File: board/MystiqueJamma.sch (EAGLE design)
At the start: 75 parts, among them IC1 7805, IC2 74LS245N, IC4 74LS245N, IC5 CY7C1049CV33, IC6 TDA1543T

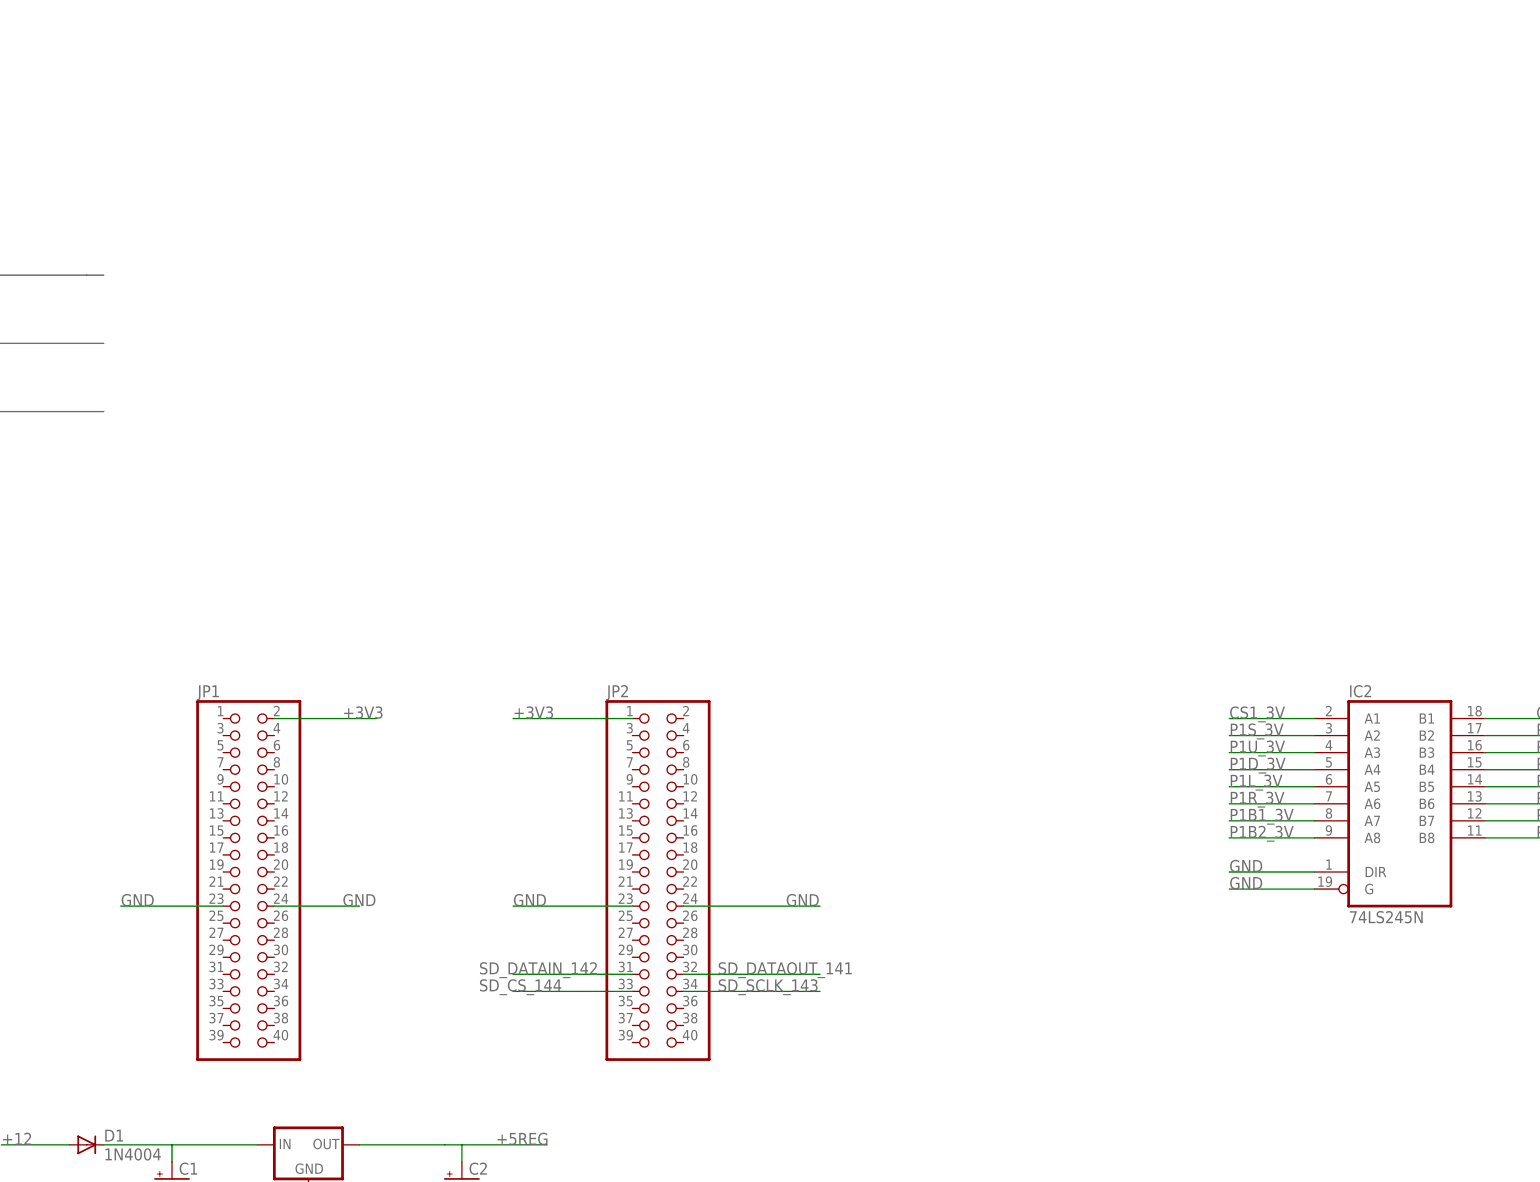
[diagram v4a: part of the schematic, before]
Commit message: included the FPGA board library
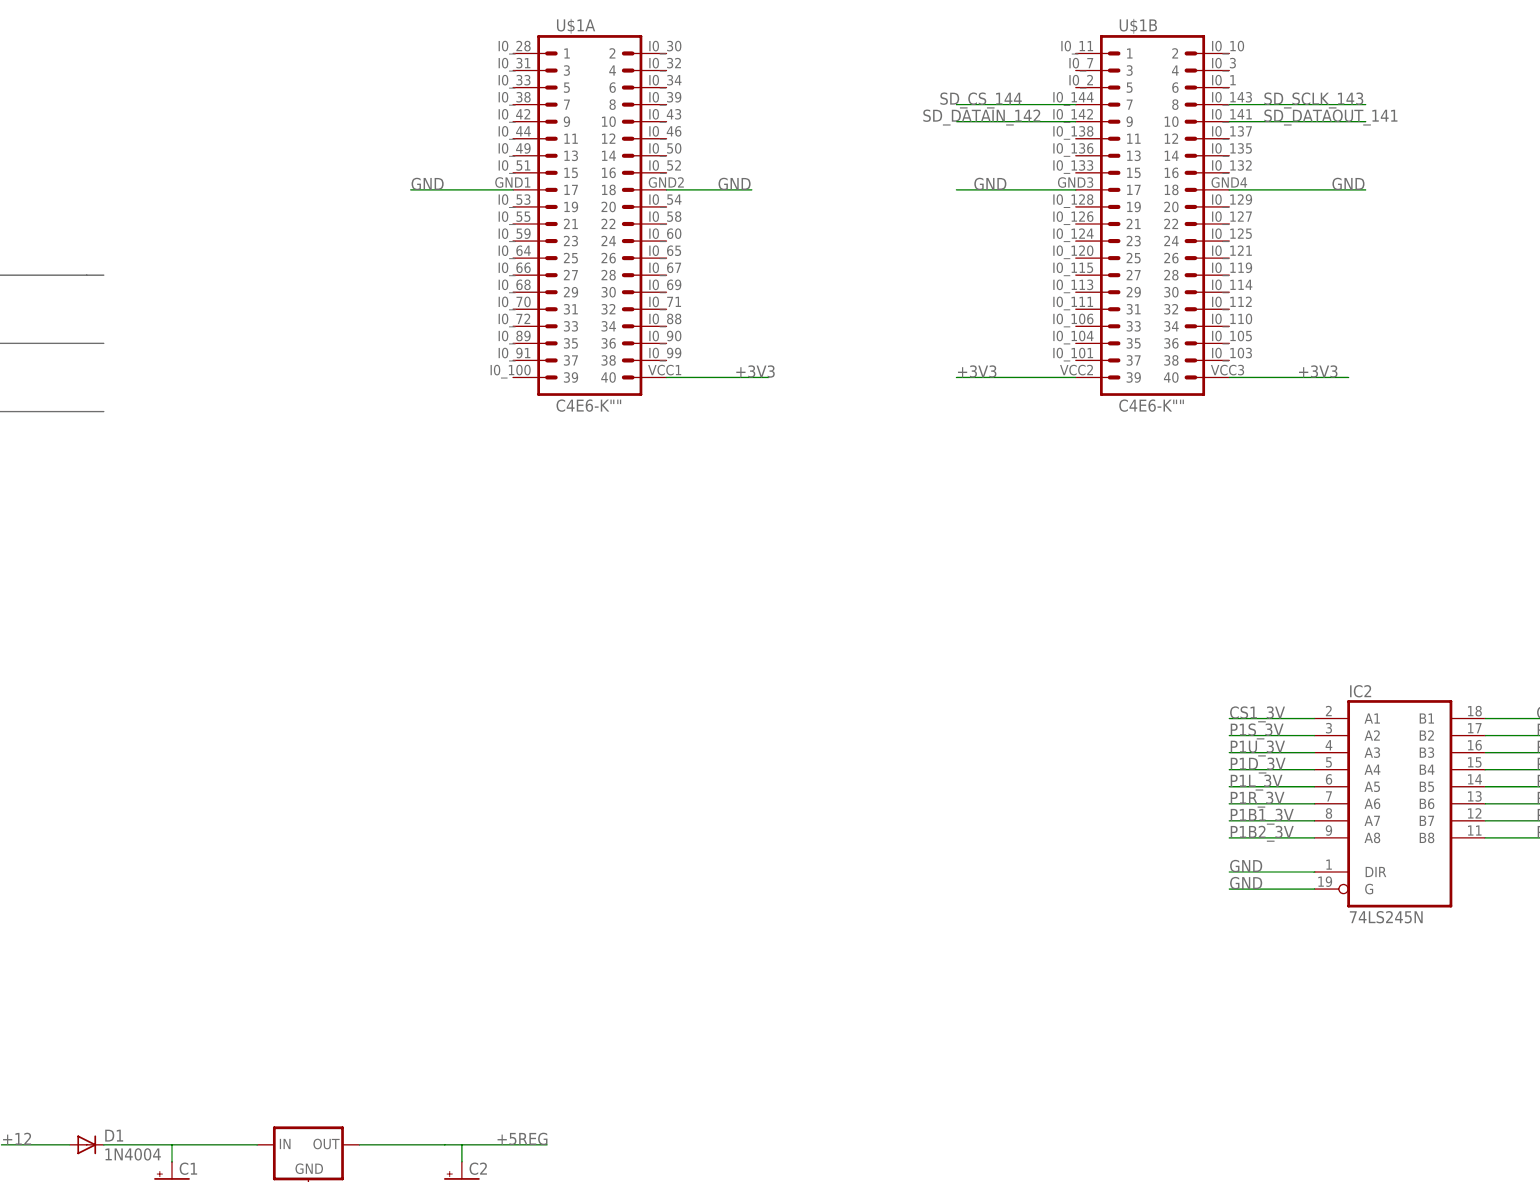
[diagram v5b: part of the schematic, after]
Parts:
- removed JP1, JP2: (no value), pinhead:PINHD-2X20
- added U$1: C4E6-K"", FPGA-BOARD:C4E6-K""
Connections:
- net +3V3: now also U$1A.40, U$1B.39; no longer JP1.2, JP2.1
- net GND: now also U$1A.17, U$1A.18, U$1B.17, U$1B.18; no longer JP1.23, JP1.24, JP2.23, JP2.24
- net SD_CS_144: now also U$1B.7; no longer JP2.33
- net SD_DATAIN_142: now also U$1B.9; no longer JP2.31
- net SD_DATAOUT_141: now also U$1B.10; no longer JP2.32
- net SD_SCLK_143: now also U$1B.8; no longer JP2.34
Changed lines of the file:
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@@
 </classes>
 <parts>
-<part name="JP1" library="pinhead" deviceset="PINHD-2X20" device=""/>
-<part name="JP2" library="pinhead" deviceset="PINHD-2X20" device=""/>
 <part name="IC1" library="SparkFun" deviceset="V_REG_78XX" device="SINK" value="7805"/>
 <part name="C1" library="rcl-2" deviceset="CPOL-US" device="E2.5-5" value="10uF"/>
@@
 <part name="R56" library="adafruit" deviceset="R-US_" device="0207/7" value="220"/>
 <part name="R57" library="adafruit" deviceset="R-US_" device="0207/7" value="220"/>
+<part name="U$1" library="FPGA-BOARD" deviceset="C4E6-K" device="&quot;&quot;"/>
 </parts>
 <sheets>
@@
 </plain>
 <instances>
-<instance part="JP1" gate="A" x="17.78" y="58.42"/>
-<instance part="JP2" gate="A" x="78.74" y="58.42"/>
 <instance part="IC1" gate="G$1" x="27.94" y="17.78"/>
 <instance part="C1" gate="G$1" x="7.62" y="12.7"/>
@@
 <instance part="R56" gate="G$1" x="-231.14" y="43.18"/>
 <instance part="R57" gate="G$1" x="-144.78" y="43.18"/>
+<instance part="U$1" gate="A" x="68.58" y="157.48"/>
+<instance part="U$1" gate="B" x="152.4" y="157.48"/>
 </instances>
 <busses>
@@
 <net name="GND" class="0">
 <segment>
-<pinref part="JP1" gate="A" pin="23"/>
-<wire x1="15.24" y1="53.34" x2="0" y2="53.34" width="0.1524" layer="91"/>
-<label x="0" y="53.34" size="1.778" layer="95"/>
-</segment>
-<segment>
-<pinref part="JP1" gate="A" pin="24"/>
-<wire x1="22.86" y1="53.34" x2="35.56" y2="53.34" width="0.1524" layer="91"/>
-<label x="33.02" y="53.34" size="1.778" layer="95"/>
-</segment>
-<segment>
-<pinref part="JP2" gate="A" pin="23"/>
-<wire x1="76.2" y1="53.34" x2="58.42" y2="53.34" width="0.1524" layer="91"/>
-<label x="58.42" y="53.34" size="1.778" layer="95"/>
-</segment>
-<segment>
-<pinref part="JP2" gate="A" pin="24"/>
-<wire x1="83.82" y1="53.34" x2="104.14" y2="53.34" width="0.1524" layer="91"/>
-<label x="99.06" y="53.34" size="1.778" layer="95"/>
+<wire x1="58.42" y1="160.02" x2="43.18" y2="160.02" width="0.1524" layer="91"/>
+<label x="43.18" y="160.02" size="1.778" layer="95"/>
+<pinref part="U$1" gate="A" pin="17"/>
+</segment>
+<segment>
+<wire x1="81.28" y1="160.02" x2="93.98" y2="160.02" width="0.1524" layer="91"/>
+<label x="88.9" y="160.02" size="1.778" layer="95"/>
+<pinref part="U$1" gate="A" pin="18"/>
+</segment>
+<segment>
+<wire x1="142.24" y1="160.02" x2="124.46" y2="160.02" width="0.1524" layer="91"/>
+<label x="127" y="160.02" size="1.778" layer="95"/>
+<pinref part="U$1" gate="B" pin="17"/>
+</segment>
+<segment>
+<wire x1="165.1" y1="160.02" x2="185.42" y2="160.02" width="0.1524" layer="91"/>
+<label x="180.34" y="160.02" size="1.778" layer="95"/>
+<pinref part="U$1" gate="B" pin="18"/>
 </segment>
 <segment>
@@
 </segment>
 <segment>
-<pinref part="JP1" gate="A" pin="2"/>
-<wire x1="22.86" y1="81.28" x2="38.1" y2="81.28" width="0.1524" layer="91"/>
-<label x="33.02" y="81.28" size="1.778" layer="95"/>
-</segment>
-<segment>
-<pinref part="JP2" gate="A" pin="1"/>
-<wire x1="76.2" y1="81.28" x2="58.42" y2="81.28" width="0.1524" layer="91"/>
-<label x="58.42" y="81.28" size="1.778" layer="95"/>
+<wire x1="81.28" y1="132.08" x2="96.52" y2="132.08" width="0.1524" layer="91"/>
+<label x="91.44" y="132.08" size="1.778" layer="95"/>
+<pinref part="U$1" gate="A" pin="40"/>
+</segment>
+<segment>
+<wire x1="142.24" y1="132.08" x2="124.46" y2="132.08" width="0.1524" layer="91"/>
+<label x="124.46" y="132.08" size="1.778" layer="95"/>
+<pinref part="U$1" gate="B" pin="39"/>
 </segment>
 <segment>
@@
 <wire x1="226.06" y1="-7.62" x2="226.06" y2="-2.54" width="0.1524" layer="91"/>
 <label x="223.52" y="-2.54" size="1.778" layer="95"/>
+</segment>
+<segment>
+<wire x1="182.88" y1="132.08" x2="165.1" y2="132.08" width="0.1524" layer="91"/>
+<label x="175.26" y="132.08" size="1.778" layer="95"/>
 </segment>
 </net>
@@
 </segment>
 <segment>
-<pinref part="JP2" gate="A" pin="33"/>
-<wire x1="76.2" y1="40.64" x2="58.42" y2="40.64" width="0.1524" layer="91"/>
-<label x="53.34" y="40.64" size="1.778" layer="95"/>
+<wire x1="142.24" y1="172.72" x2="124.46" y2="172.72" width="0.1524" layer="91"/>
+<label x="121.92" y="172.72" size="1.778" layer="95"/>
+<pinref part="U$1" gate="B" pin="7"/>
 </segment>
 </net>
@@
 </segment>
 <segment>
-<pinref part="JP2" gate="A" pin="34"/>
-<wire x1="83.82" y1="40.64" x2="104.14" y2="40.64" width="0.1524" layer="91"/>
-<label x="88.9" y="40.64" size="1.778" layer="95"/>
+<wire x1="165.1" y1="172.72" x2="185.42" y2="172.72" width="0.1524" layer="91"/>
+<label x="170.18" y="172.72" size="1.778" layer="95"/>
+<pinref part="U$1" gate="B" pin="8"/>
 </segment>
 </net>
@@
 </segment>
 <segment>
-<pinref part="JP2" gate="A" pin="31"/>
-<wire x1="76.2" y1="43.18" x2="58.42" y2="43.18" width="0.1524" layer="91"/>
-<label x="53.34" y="43.18" size="1.778" layer="95"/>
+<wire x1="142.24" y1="170.18" x2="124.46" y2="170.18" width="0.1524" layer="91"/>
+<label x="119.38" y="170.18" size="1.778" layer="95"/>
+<pinref part="U$1" gate="B" pin="9"/>
 </segment>
 </net>
@@
 </segment>
 <segment>
-<pinref part="JP2" gate="A" pin="32"/>
-<wire x1="83.82" y1="43.18" x2="104.14" y2="43.18" width="0.1524" layer="91"/>
-<label x="88.9" y="43.18" size="1.778" layer="95"/>
+<wire x1="165.1" y1="170.18" x2="185.42" y2="170.18" width="0.1524" layer="91"/>
+<label x="170.18" y="170.18" size="1.778" layer="95"/>
+<pinref part="U$1" gate="B" pin="10"/>
 </segment>
 </net>
@@
 <pinref part="R37" gate="G$1" pin="2"/>
 <junction x="-149.86" y="88.9"/>
-<pinref part="R37" gate="G$1" pin="2"/>
 <wire x1="-149.86" y1="88.9" x2="-149.86" y2="91.44" width="0.1524" layer="91"/>
 <junction x="-149.86" y="91.44"/>
@@
 <pinref part="R38" gate="G$1" pin="2"/>
 <junction x="-149.86" y="73.66"/>
-<pinref part="R38" gate="G$1" pin="2"/>
 <wire x1="-149.86" y1="73.66" x2="-149.86" y2="76.2" width="0.1524" layer="91"/>
 <junction x="-149.86" y="76.2"/>

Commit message: docs
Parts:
- B1: value C4E6-K"" -> (none)
- renumbered U$1 to B1
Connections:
- net +3V3: now also B1B.40
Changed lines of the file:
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@@
 <part name="R56" library="adafruit" deviceset="R-US_" device="0207/7" value="220"/>
 <part name="R57" library="adafruit" deviceset="R-US_" device="0207/7" value="220"/>
-<part name="U$1" library="FPGA-BOARD" deviceset="C4E6-K" device="&quot;&quot;"/>
+<part name="B1" library="FPGA-BOARD" deviceset="C4E6-K" device="&quot;&quot;"/>
 </parts>
 <sheets>
@@
 <instance part="R56" gate="G$1" x="-231.14" y="43.18"/>
 <instance part="R57" gate="G$1" x="-144.78" y="43.18"/>
-<instance part="U$1" gate="A" x="68.58" y="157.48"/>
-<instance part="U$1" gate="B" x="152.4" y="157.48"/>
+<instance part="B1" gate="A" x="68.58" y="157.48"/>
+<instance part="B1" gate="B" x="152.4" y="157.48"/>
 </instances>
 <busses>
@@
 <wire x1="58.42" y1="160.02" x2="43.18" y2="160.02" width="0.1524" layer="91"/>
 <label x="43.18" y="160.02" size="1.778" layer="95"/>
-<pinref part="U$1" gate="A" pin="17"/>
+<pinref part="B1" gate="A" pin="17"/>
 </segment>
 <segment>
 <wire x1="81.28" y1="160.02" x2="93.98" y2="160.02" width="0.1524" layer="91"/>
 <label x="88.9" y="160.02" size="1.778" layer="95"/>
-<pinref part="U$1" gate="A" pin="18"/>
+<pinref part="B1" gate="A" pin="18"/>
 </segment>
 <segment>
 <wire x1="142.24" y1="160.02" x2="124.46" y2="160.02" width="0.1524" layer="91"/>
 <label x="127" y="160.02" size="1.778" layer="95"/>
-<pinref part="U$1" gate="B" pin="17"/>
+<pinref part="B1" gate="B" pin="17"/>
 </segment>
 <segment>
 <wire x1="165.1" y1="160.02" x2="185.42" y2="160.02" width="0.1524" layer="91"/>
 <label x="180.34" y="160.02" size="1.778" layer="95"/>
-<pinref part="U$1" gate="B" pin="18"/>
+<pinref part="B1" gate="B" pin="18"/>
 </segment>
 <segment>
@@
 <wire x1="81.28" y1="132.08" x2="96.52" y2="132.08" width="0.1524" layer="91"/>
 <label x="91.44" y="132.08" size="1.778" layer="95"/>
-<pinref part="U$1" gate="A" pin="40"/>
+<pinref part="B1" gate="A" pin="40"/>
 </segment>
 <segment>
 <wire x1="142.24" y1="132.08" x2="124.46" y2="132.08" width="0.1524" layer="91"/>
 <label x="124.46" y="132.08" size="1.778" layer="95"/>
-<pinref part="U$1" gate="B" pin="39"/>
+<pinref part="B1" gate="B" pin="39"/>
 </segment>
 <segment>
@@
 <wire x1="182.88" y1="132.08" x2="165.1" y2="132.08" width="0.1524" layer="91"/>
 <label x="175.26" y="132.08" size="1.778" layer="95"/>
+<pinref part="B1" gate="B" pin="40"/>
 </segment>
 </net>
@@
 <wire x1="142.24" y1="172.72" x2="124.46" y2="172.72" width="0.1524" layer="91"/>
 <label x="121.92" y="172.72" size="1.778" layer="95"/>
-<pinref part="U$1" gate="B" pin="7"/>
+<pinref part="B1" gate="B" pin="7"/>
 </segment>
 </net>
@@
 <wire x1="165.1" y1="172.72" x2="185.42" y2="172.72" width="0.1524" layer="91"/>
 <label x="170.18" y="172.72" size="1.778" layer="95"/>
-<pinref part="U$1" gate="B" pin="8"/>
+<pinref part="B1" gate="B" pin="8"/>
 </segment>
 </net>
@@
 <wire x1="142.24" y1="170.18" x2="124.46" y2="170.18" width="0.1524" layer="91"/>
 <label x="119.38" y="170.18" size="1.778" layer="95"/>
-<pinref part="U$1" gate="B" pin="9"/>
+<pinref part="B1" gate="B" pin="9"/>
 </segment>
 </net>
@@
 <wire x1="165.1" y1="170.18" x2="185.42" y2="170.18" width="0.1524" layer="91"/>
 <label x="170.18" y="170.18" size="1.778" layer="95"/>
-<pinref part="U$1" gate="B" pin="10"/>
-</segment>
-</net>
+<pinref part="B1" gate="B" pin="10"/>
+</segment>
+</net>
